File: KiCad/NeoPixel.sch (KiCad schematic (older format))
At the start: 0 parts

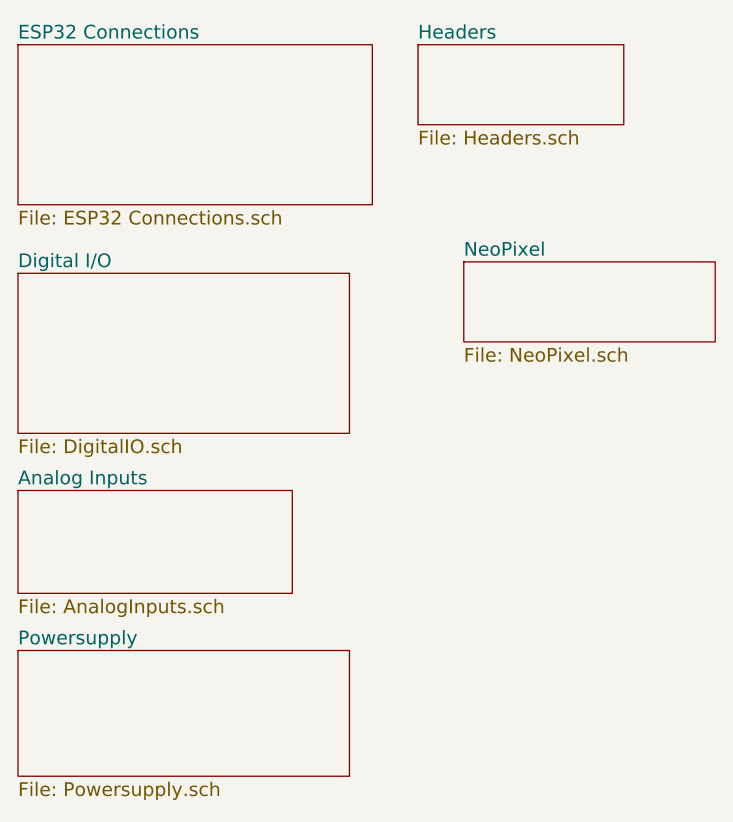
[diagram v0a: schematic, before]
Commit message: Reworked power-supply to provide 5V. Updated ESP-connections.
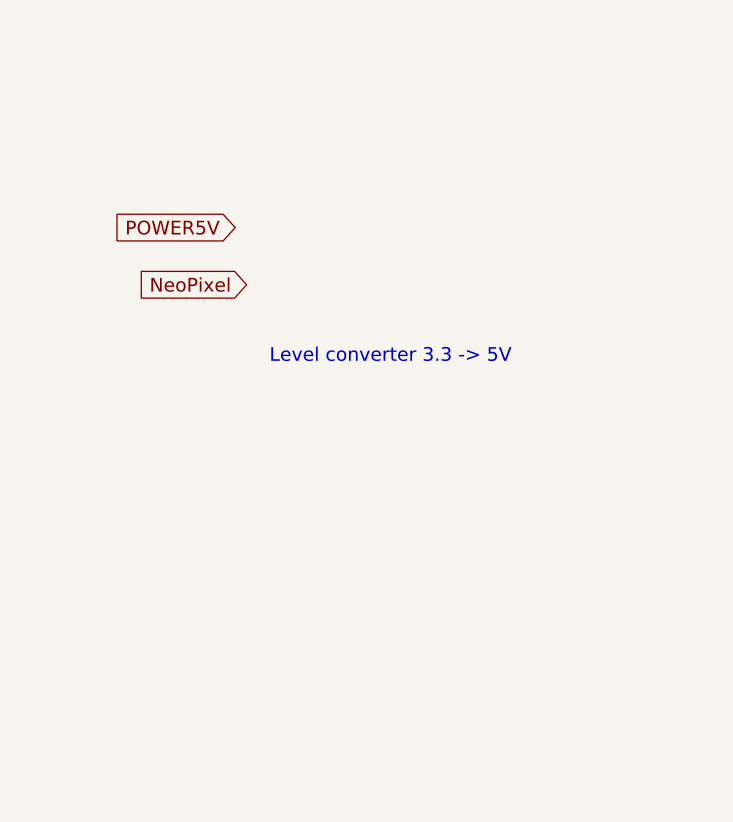
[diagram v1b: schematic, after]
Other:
- note added: "Level converter 3.3 -> 5V"
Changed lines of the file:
@@
 $Descr A4 11693 8268
 encoding utf-8
-Sheet 1 7
+Sheet 7 7
 Title ""
 Date ""
@@
 Comment4 ""
 $EndDescr
-$Sheet
-S 900  1800 1450 700
-U 591810E7
-F0 "Digital I/O" 60
-F1 "DigitalIO.sch" 60
-$EndSheet
-$Sheet
-S 900  800  1550 700
-U 59181FE5
-F0 "ESP32 Connections" 60
-F1 "ESP32 Connections.sch" 60
-$EndSheet
-$Sheet
-S 900  2750 1200 450
-U 591A7DC8
-F0 "Analog Inputs" 60
-F1 "AnalogInputs.sch" 60
-$EndSheet
-$Sheet
-S 900  3450 1450 550
-U 591CB050
-F0 "Powersupply" 60
-F1 "Powersupply.sch" 60
-$EndSheet
-$Sheet
-S 2650 800  900  350
-U 5924A2C7
-F0 "Headers" 60
-F1 "Headers.sch" 60
-$EndSheet
-$Sheet
-S 2850 1750 1100 350
-U 5924F41E
-F0 "NeoPixel" 60
-F1 "NeoPixel.sch" 60
-$EndSheet
+Text GLabel 1850 1600 0    60   Input ~ 0
+POWER5V
+Text GLabel 1900 1850 0    60   Input ~ 0
+NeoPixel
+Text Notes 2000 2200 0    60   ~ 0
+Level converter 3.3 -> 5V
 $EndSCHEMATC

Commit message: More work
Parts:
- added C701, C702, C703, C704: 100nF, Capacitors_SMD:C_0805, symbol C
- added J701, J704, J705, J706: NEO1, Pin_Headers:Pin_Header_Straight_1x04_Pitch1.27mm, symbol CONN_01X04_FEMALE
- added J702: 5V_I/O_2, Pin_Headers:Pin_Header_Straight_1x02_Pitch2.54mm, symbol CONN_01X02
- added J703: 5V_I/O_1, Pin_Headers:Pin_Header_Straight_1x02_Pitch2.54mm, symbol CONN_01X02
- added J707: NeoPixel, Pin_Headers:Pin_Header_Straight_1x01_Pitch2.54mm, symbol CONN_01X01
- added R701: 10k, Resistors_SMD:R_0805, symbol R
- added U701: TXB0102DCT, Housings_SSOP:TSSOP-8_3x3mm_Pitch0.65mm, symbol TXB0102DCT
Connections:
- net POWER5V: now also J701.2, J704.2, J705.2, J706.2, U701.7 (VCCB)
- new net: C703.1, J702.1 (P1), U701.1 (B2)
- new net: C704.1, J701.1, J703.1 (P1), U701.8 (B1)
- new net: J701.4, J704.1
- new net: J704.4, J705.1
- new net: J705.4, J706.1
- new net: J706.4, J707.1 (P1)
- new net 5V_I/O_1: C701.1, U701.5 (A1)
- new net 5V_I/O_2: C702.1, U701.4 (A2)
- new net 5V_I/O_Enable: R701.1, U701.6 (OE)
- new net GND: C701.2, C702.2, C703.2, C704.2, J701.3, J702.2 (P2), J703.2 (P2), J704.3, J705.3, J706.3, R701.2, U701.2 (GND)
- new net POWER3V3: U701.3 (VCCA)
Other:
- note removed: "Level converter 3.3 -> 5V"
